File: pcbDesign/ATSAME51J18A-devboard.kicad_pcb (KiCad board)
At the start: 2 copper layers, 82.3 x 29.2 mm, 74 parts, among them J1 Micro_SD_Card, J10 CAN, J11 Conn_01x32_Male, J2 BAT, J3 QWIIC, J7 Conn_01x32_Male, J9 USB4105_REVA, SW1 RST, U1 TCAN1051GVDRQ1, U2 ATSAME51J18A-A, U3 MIC5219-5.0YMM, U4 LM27762, U5 LM2775QDSGTQ1, U6 SC630AULTRT, U7 BQ24074RGT, U8 BQ27441DRZR-G1B, Y1 32.768

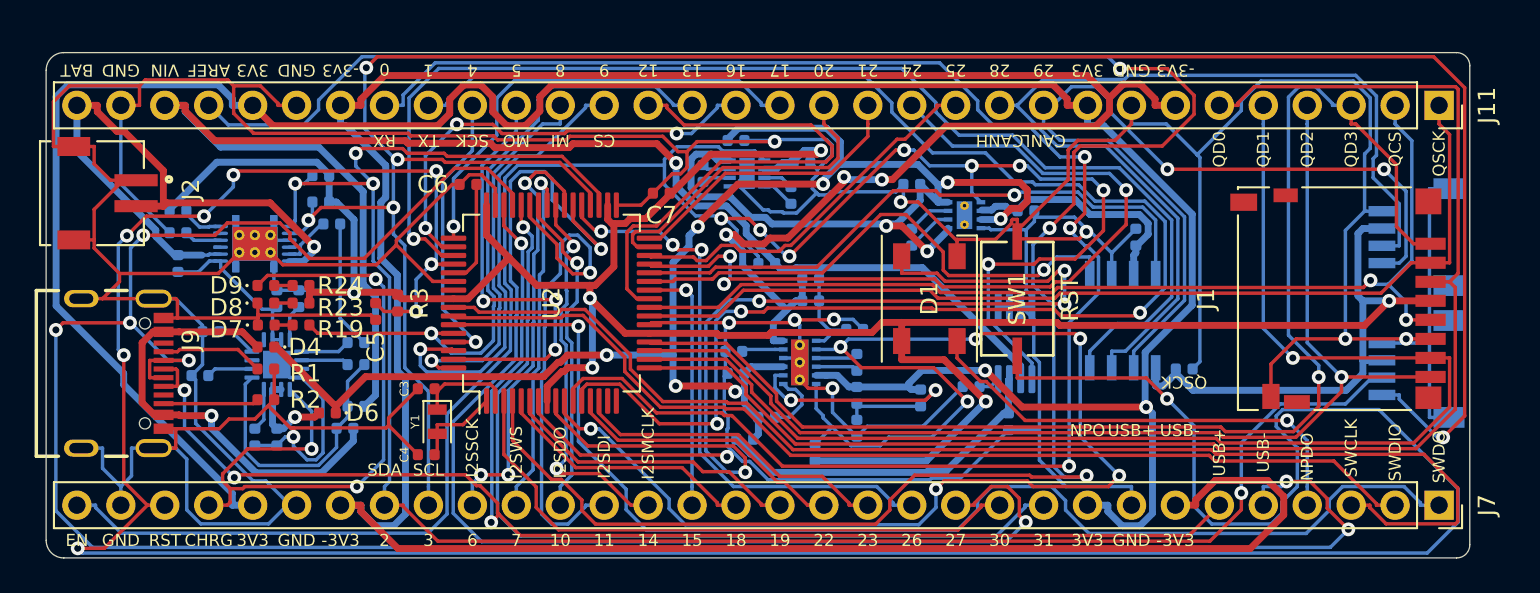
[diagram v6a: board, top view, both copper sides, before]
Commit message: Corrected pin header spacing to fit on a bread board
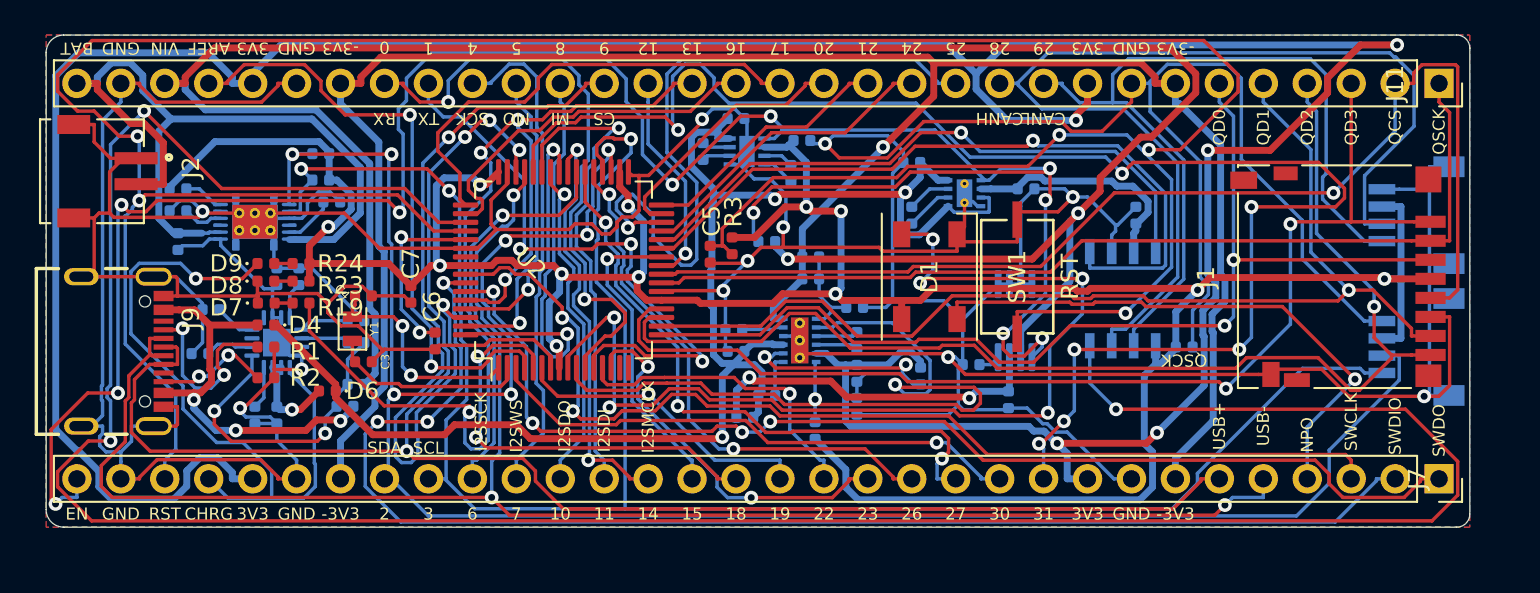
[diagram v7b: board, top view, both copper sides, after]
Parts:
- moved C5 19.6 mm to (179.4, 124.2)
- moved R3 19.6 mm to (180.6, 123.7)
- moved C7 15.6 mm to (162.1, 126.5), turned to 90 degrees
- moved C4 9.87 mm to (159.3, 126.6), turned to 180 degrees
- moved C6 9.24 mm to (163.5, 129.2), turned to 90 degrees
- moved Y1 7.27 mm to (158.7, 128.5), turned to 90 degrees
- moved C3 3.95 mm to (159.3, 130.4), turned to 0 degrees
- moved U2 2.04 mm to (170.9, 125.1)
- moved J7 1.52 mm to (221.5, 137.2)
- moved C1 1.27 mm to (206.8, 129.5)
- moved C12 1.27 mm to (196.6, 132.6)
- moved C13 1.27 mm to (180.7, 128.5)
- moved C15 1.27 mm to (191.5, 131.2)
- moved C20 1.27 mm to (180.8, 116.3)
- moved C21 1.27 mm to (178.9, 118.2)
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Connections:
- U5 pad V: (no net) -> GND
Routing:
- net AREF: track 130.5 -> 35.5 mm, vias 3 -> 2
- net CAN_S: track 71.1 -> 155.6 mm, vias 1 -> 3
- net VBUS_-3V3_CH2_REG: track 183.7 -> 119.5 mm, vias 3 -> 1
- net 0[Rx0]: track 95.8 -> 34.9 mm, vias 3 -> 2
- net 1[Tx0]: track 93.8 -> 35.4 mm
- net VBUS_VIN_NREG: track 84.7 -> 128.5 mm, vias 1 -> 2
- net VBUS_3V3_CH1_REG: track 149.4 -> 192.6 mm, vias 2 -> 5
- net EN_2: track 84.7 -> 46.4 mm, vias 7 -> 2
- net 31: track 51.8 -> 89.8 mm, vias 1 -> 7
- net USB_N: track 138.4 -> 101.6 mm, vias 6 -> 3
- net 27: track 72.3 -> 36.0 mm, vias 2 -> 3
- net 24: track 48.2 -> 18.1 mm, vias 3 -> 0
- net 13: track 37.9 -> 62.2 mm, vias 1 -> 4
- net VBUS_NREG: track 108.2 -> 85.6 mm, vias 9 -> 3
- net QDAT0: track 84.0 -> 61.5 mm, vias 0 -> 2
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- added copper zone on F.Cu, net (none)
- added copper zone on B.Cu, net GND
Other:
- board size 82.3 x 29.2 mm -> 82.3 x 28.4 mm
- board text removed: "NPDO"

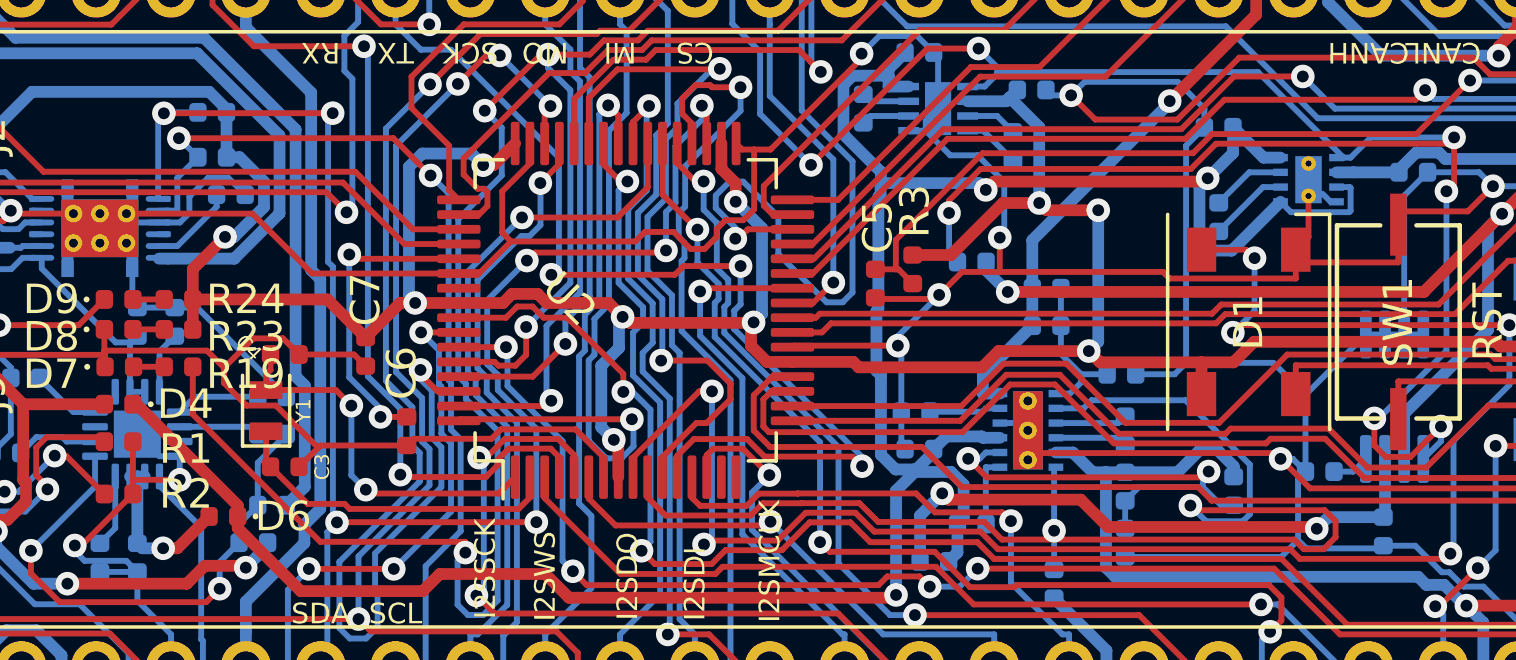
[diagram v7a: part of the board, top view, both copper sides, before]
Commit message: Reconfigured charging circuit
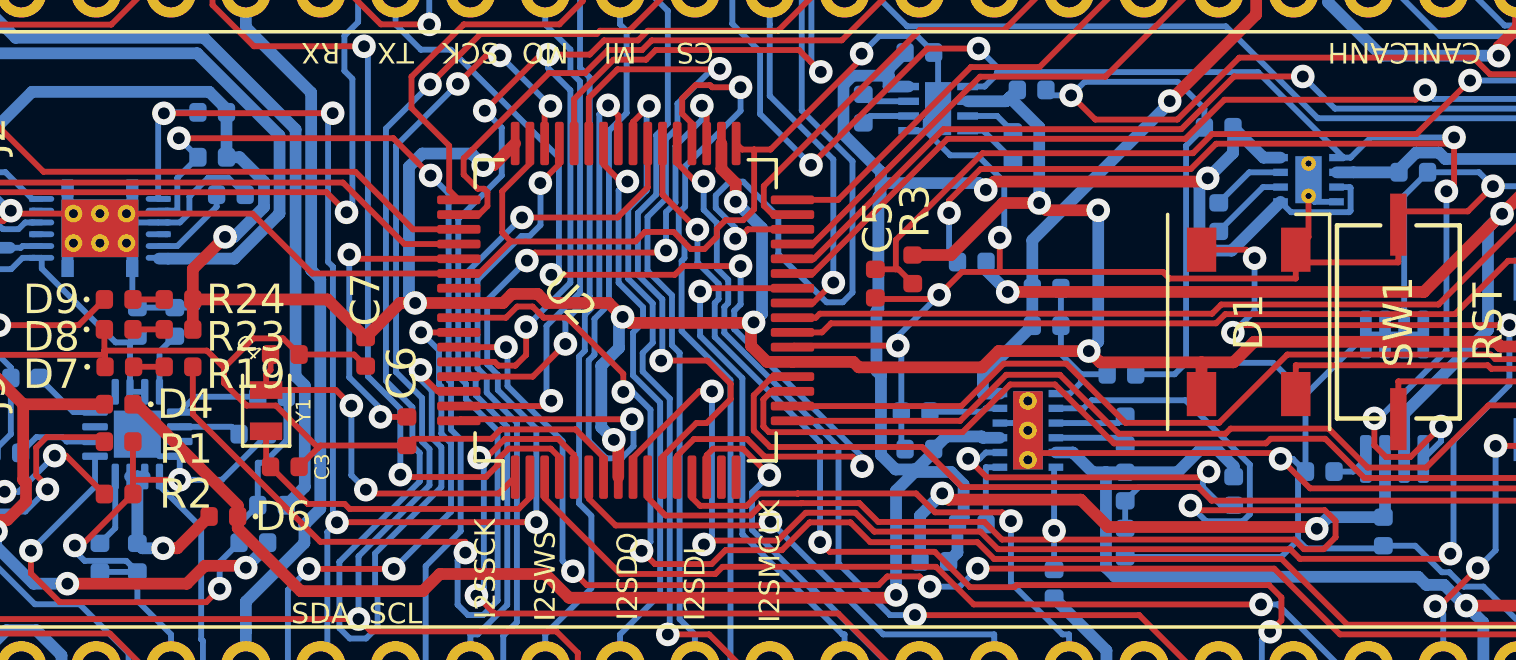
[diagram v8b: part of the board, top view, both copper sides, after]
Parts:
- moved R20 0.64 mm to (158.2, 129.3)
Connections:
- R20 pad 1: Net-(D2-Pad1) -> GND
- R21 pad 2: GND -> Net-(D2-Pad1)
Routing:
- net Net-(D2-Pad1): track 18.1 -> 19.5 mm
- net CHARGE_MODE_CH0: track 2.75 -> 2.12 mm
- net GND: track 445.9 -> 446.4 mm
- added copper zone on F.Cu, net GND
- removed copper zone on F.Cu, net (none)
